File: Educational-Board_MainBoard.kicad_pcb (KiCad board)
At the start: 2 copper layers, 164.5 x 75 mm, 209 parts, among them J201 Screw_Terminal_01x02_P5mm, J202 USB-C_304A-ACP16X, J401 ACC_INT1, J402 BME_SPI, J403 LUX_INT, J501 RGB_OUT, J601 PWR_IN1, J602 PWR_IN2, J603 PWR_IN3, J604 PWR_IN4, J605 MCP_INT, J606 5V, J607 GND, J608 3V3, J609 EX_PA, J610 EX_PB, J611 PWR_OUT1, J612 PWR_OUT3, J613 PWR_OUT2, J614 PWR_OUT4, Q501 AO3400A, Q601 IRLML9301TRPBF, Q602 IRLML9301TRPBF, Q603 IRLML9301TRPBF, Q604 IRLML9301TRPBF, SW301 RESET, SW501 BUTTON1, SW502 BUTTON2, SW503 BUTTON3, SW504 BUTTON4, SW505 BUTTON5, U201 TPS5430DDA, U202 NUCLEO64-H503RB, U401 LSM6DS3, U402 BME280, U403 OPT4001, U404 INA2180A2, U406 YK16S-L7.2-B10Ka(32-8)-G-A29, U501 74LVC1G34, U502 SSD1315 OLED 0.98", U601 TLP291-4, U602 TLP291-4, U603 MCP23017_SS

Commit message: Continued the routing
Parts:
- removed the H102 at (236.0, 53.5)
- removed the H103 at (236.0, 121.5)
- removed kibuzzard-69F9CDB6: G***, kibuzzard-69F9CDB6
- added kibuzzard-69FB5140: G***, kibuzzard-69FB5140, F.Cu at (80.3, 56.6)
- added kibuzzard-69FB71BC: G***, kibuzzard-69FB71BC, F.Cu at (225.5, 58.5)
- added kibuzzard-69FB71E5: G***, kibuzzard-69FB71E5, F.Cu at (225.5, 61.2)
- moved R509 72.9 mm to (194.8, 71.5), turned to -90 degrees
- moved C504 71.2 mm to (197.6, 71.5), turned to 90 degrees
- moved R507 64.3 mm to (197.6, 75.1), turned to 90 degrees
- moved R510 56.3 mm to (223.6, 80.7), turned to 0 degrees
- moved C505 56.3 mm to (223.6, 77.7)
- moved R508 55.2 mm to (223.6, 79.2), turned to 0 degrees
- moved R501 40.2 mm to (203.1, 113.1), turned to 180 degrees
- moved R503 39.4 mm to (199.7, 115.8), turned to 0 degrees
- moved R504 37.0 mm to (188.6, 103.5), turned to 0 degrees
- moved C502 36.8 mm to (192.0, 100.8)
- moved R502 36.8 mm to (188.6, 100.8)
- moved C501 36.3 mm to (199.7, 113.1), turned to 180 degrees
- moved SW501 30.0 mm to (207.0, 105.5)
- moved SW503 30.0 mm to (207.0, 75.5)
- moved H102 20.0 mm to (226.5, 53.5)
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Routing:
- net /MCU/BTN_4: track 0.00 -> 194.1 mm, vias 0 -> 2
- net +3V3: track 302.7 -> 410.3 mm, vias 9 -> 6
- net Net-(C506-Pad1): track 3.25 -> 89.0 mm, vias 0 -> 4
- net /MCU/BTN_3: track 0.06 -> 48.1 mm, vias 0 -> 1
- net /UI/BUZZER: track 25.7 -> 63.5 mm
- net /MCU/BTN_1: track 65.0 -> 92.9 mm
- net Net-(C501-Pad1): track 0.00 -> 15.5 mm
- net /MCU/BTN_2: track 0.00 -> 12.6 mm, vias 0 -> 1
- net /MCU/I2C_SCL: track 156.8 -> 166.1 mm, vias 2 -> 4
- net Net-(C502-Pad1): track 0.00 -> 7.48 mm
- net /MCU/I2C_SDA: track 164.4 -> 171.8 mm, vias 4 -> 6
- net Net-(C505-Pad1): track 0.00 -> 5.69 mm
- net Net-(C504-Pad1): track 0.00 -> 5.32 mm
- net /MCU/JOYSTICK_X: track 35.9 -> 40.8 mm
- net /MCU/JOYSTICK_Y: track 21.7 -> 25.5 mm
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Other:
- board size 164.5 x 75 mm -> 155 x 75 mm
- board text added: "C202>5"
- board text added: "C206>8"
- board text added: "R613>16"
- board text removed: "C202-5"
- board text removed: "C206-8"

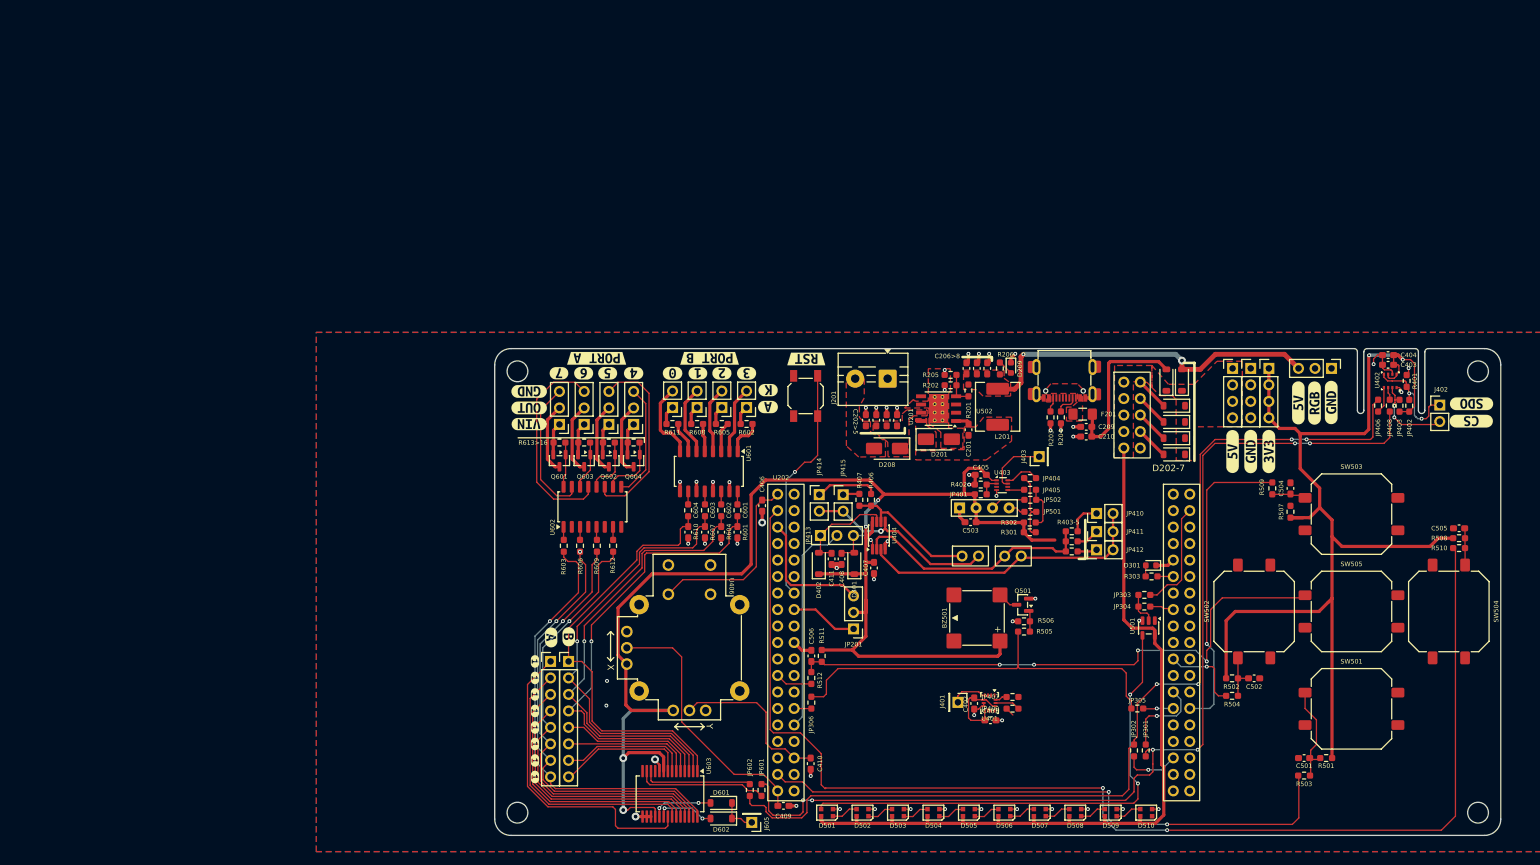
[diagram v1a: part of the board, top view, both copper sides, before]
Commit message: Finished the routing: TODO fixing IMU
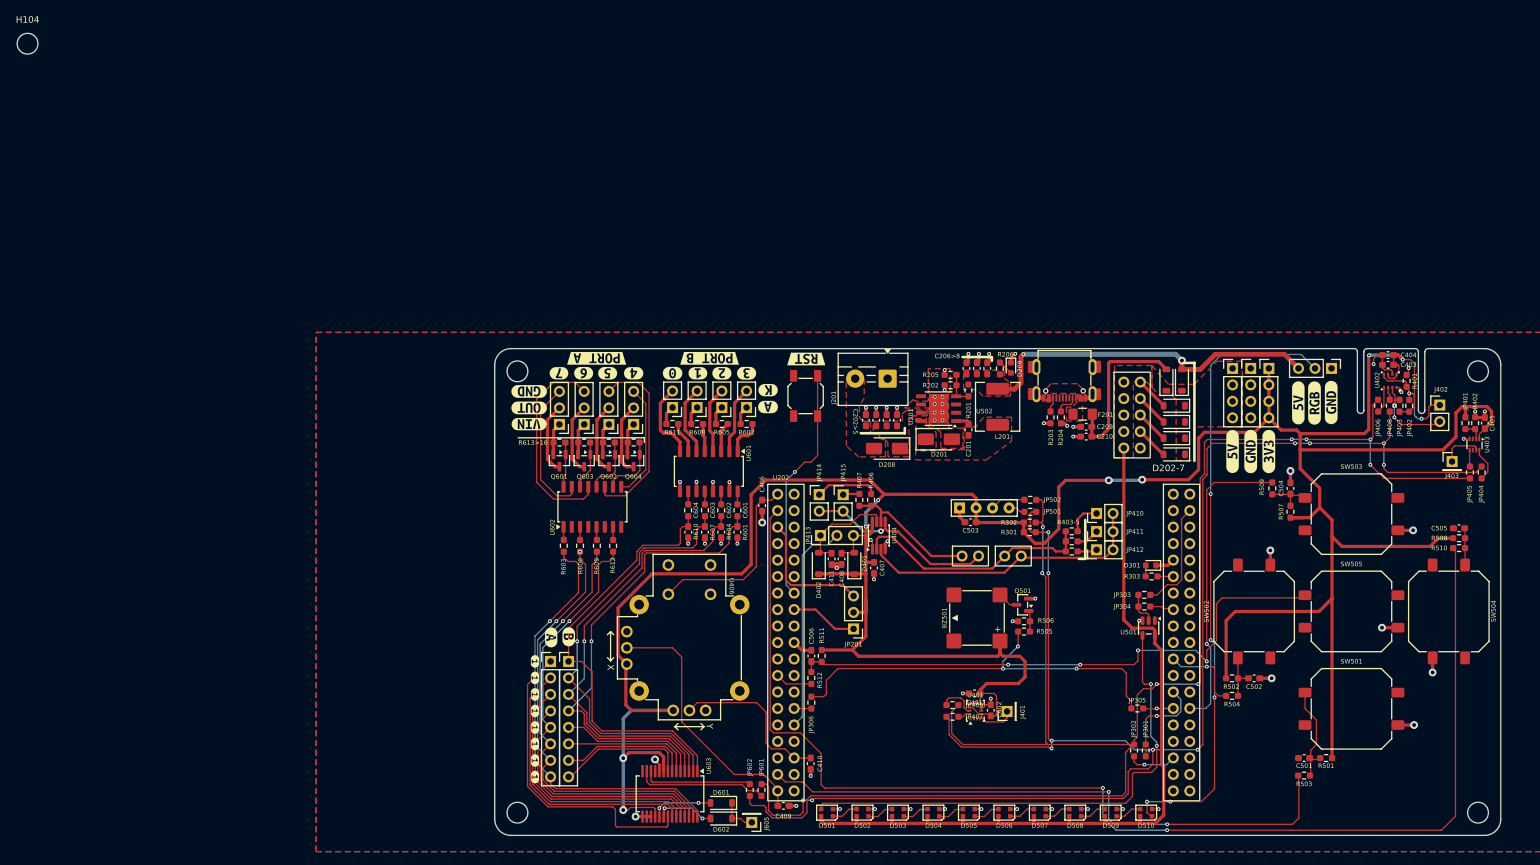
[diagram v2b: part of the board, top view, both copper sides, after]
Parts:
- removed kibuzzard-69FB71BC: G***, kibuzzard-69FB71BC
- removed kibuzzard-69FB71E5: G***, kibuzzard-69FB71E5
- added H104: MountingHole, MountingHole:MountingHole_3.2mm_M3_ISO14580, F.Cu at (3.02, 3.02)
- moved C405 78.1 mm to (227.6, 61.5), turned to 90 degrees
- moved R402 76.8 mm to (226.1, 61.5), turned to 90 degrees
- moved JP401 75.5 mm to (224.6, 61.5), turned to 90 degrees
- moved U403 73.0 mm to (226.0, 64.8), turned to -90 degrees
- moved JP404 69.6 mm to (227.1, 69.1), turned to 90 degrees
- moved JP405 67.8 mm to (225.3, 69.1), turned to -90 degrees
- moved J403 63.6 mm to (222.5, 67.4), turned to 0 degrees
- moved JP407 9.74 mm to (145.5, 106.7), turned to 0 degrees
- moved JP409 9.26 mm to (145.5, 104.9), turned to 0 degrees
- moved J401 7.71 mm to (153.9, 105.9), turned to 90 degrees
- moved C401 4.82 mm to (148.9, 103.1), turned to 180 degrees
- moved C402 2.76 mm to (151.4, 105.7), turned to 90 degrees
- moved U401 2.50 mm to (149.1, 105.8), turned to 90 degrees
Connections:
- U202 pad 18: +5V -> unconnected-(U202A-+5V-Pad18)
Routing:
- net /UI/RGB_OUT: track 0.00 -> 97.0 mm, vias 0 -> 5
- net +3V3: track 410.3 -> 505.4 mm, vias 6 -> 8
- net /MCU/I2C_SCL: track 166.1 -> 253.3 mm, vias 4 -> 8
- net /MCU/I2C_SDA: track 171.8 -> 257.3 mm, vias 6 -> 12
- net GND: track 81.6 -> 97.0 mm, vias 53 -> 58
- net Net-(J403-Pin_1): track 9.49 -> 6.41 mm
- net /UI/RGB_DIN: track 76.3 -> 78.6 mm
- net Net-(JP409-A): track 3.89 -> 5.84 mm
- net Net-(C504-Pad1): track 5.32 -> 7.14 mm
- net /MCU/I2C1_SCL: track 8.65 -> 7.49 mm
- net /MCU/BTN_3: track 48.1 -> 47.3 mm
- net /UI/BUZZER: track 63.5 -> 64.3 mm, vias 0 -> 3

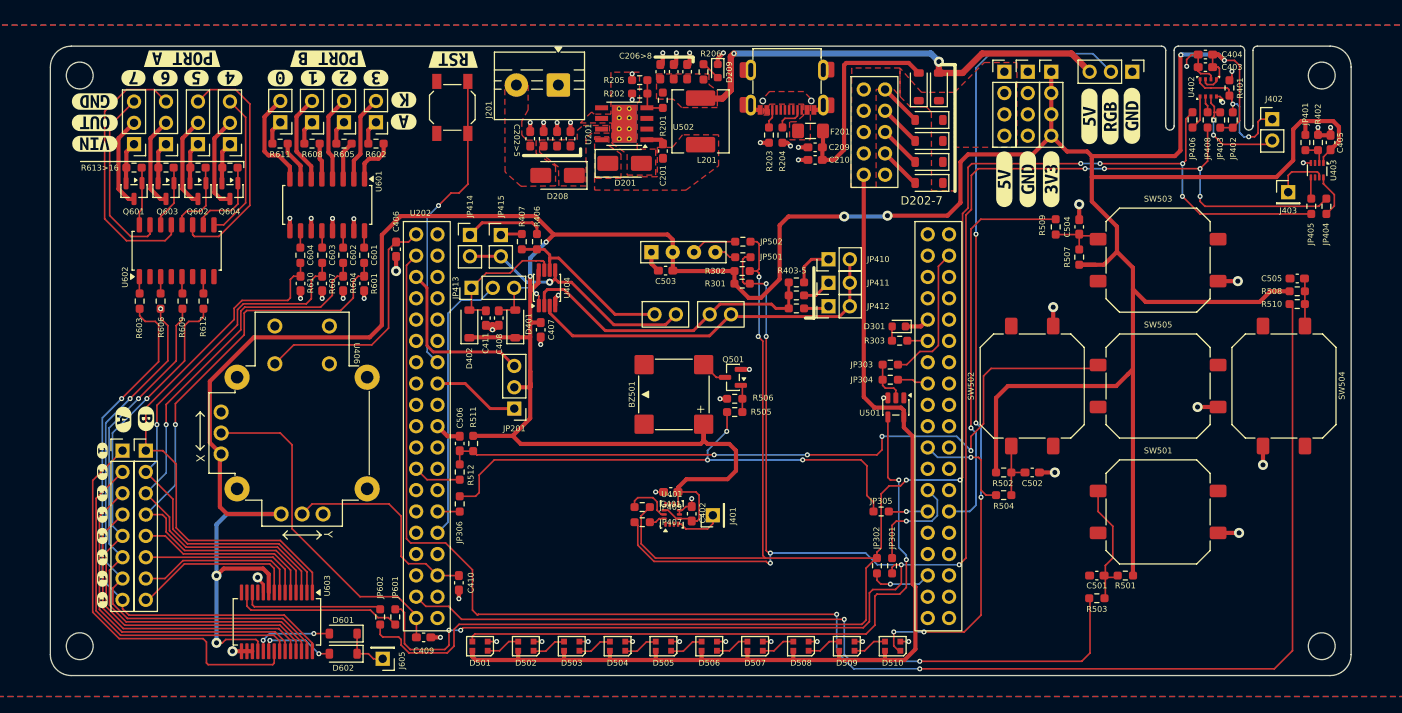
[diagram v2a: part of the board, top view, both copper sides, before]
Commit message: routing and silkscreen logo
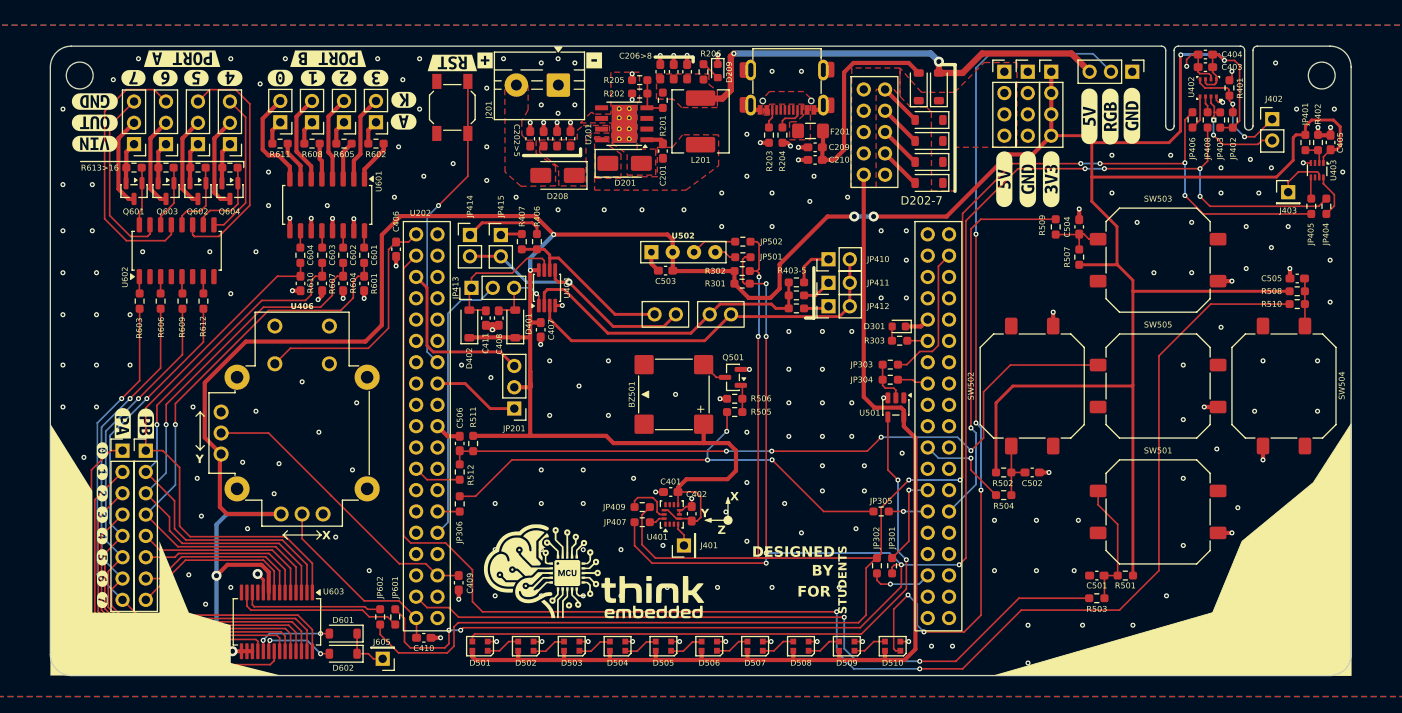
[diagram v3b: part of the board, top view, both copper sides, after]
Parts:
- removed kibuzzard-69F28E96: G***, kibuzzard-69F28E96
- removed kibuzzard-69F28EB1: G***, kibuzzard-69F28EB1
- removed kibuzzard-69F29536 (x8): G***, kibuzzard-69F29536
- added G***: LOGO, LOGO, F.Cu at (140.2, 112.2)
- added G***: LOGO, LOGO, B.Cu at (215.0, 84.1)
- added kibuzzard-69FCC61F: G***, kibuzzard-69FCC61F, F.Cu at (126.8, 51.7)
- added kibuzzard-69FCC630: G***, kibuzzard-69FCC630, F.Cu at (139.8, 51.7)
- added kibuzzard-69FCE761: G***, kibuzzard-69FCE761, F.Cu at (81.2, 98.2)
- added kibuzzard-69FCE768: G***, kibuzzard-69FCE768, F.Cu at (81.2, 100.7)
- added kibuzzard-69FCE76D: G***, kibuzzard-69FCE76D, F.Cu at (81.2, 103.3)
- added kibuzzard-69FCE770: G***, kibuzzard-69FCE770, F.Cu at (81.2, 105.8)
- added kibuzzard-69FCE773: G***, kibuzzard-69FCE773, F.Cu at (81.2, 108.4)
- added kibuzzard-69FCE777: G***, kibuzzard-69FCE777, F.Cu at (81.2, 110.9)
- added kibuzzard-69FCE77B: G***, kibuzzard-69FCE77B, F.Cu at (81.2, 113.5)
- added kibuzzard-69FCE77E: G***, kibuzzard-69FCE77E, F.Cu at (81.2, 116.0)
- added kibuzzard-69FCE792: G***, kibuzzard-69FCE792, F.Cu at (86.4, 95.0)
- added kibuzzard-69FCE79E: G***, kibuzzard-69FCE79E, F.Cu at (83.6, 94.9)
- added kibuzzard-69FCE905: G***, kibuzzard-69FCE905, B.Cu at (208.5, 99.5)
- added kibuzzard-69FCE911: G***, kibuzzard-69FCE911, B.Cu at (206.2, 108.0)
- moved C410 7.77 mm to (119.5, 120.5), turned to 0 degrees
- moved C409 7.73 mm to (123.7, 113.9), turned to -90 degrees
- moved J401 4.98 mm to (150.5, 109.5)
- moved kibuzzard-69F3BF46 0.41 mm to (122.9, 52.0)
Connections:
- C409 pad 1: /MCU/JOYSTICK_X -> /MCU/JOYSTICK_Y
- C410 pad 1: /MCU/JOYSTICK_Y -> /MCU/JOYSTICK_X
- U406 pad 2: /MCU/JOYSTICK_X -> /MCU/JOYSTICK_Y
- U406 pad 5: /MCU/JOYSTICK_Y -> /MCU/JOYSTICK_X
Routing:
- net /MCU/JOYSTICK_X: track 40.8 -> 22.8 mm
- net +3V3: track 505.4 -> 489.4 mm
- net /MCU/BTN_4: track 194.1 -> 184.2 mm
- net /MCU/JOYSTICK_Y: track 25.5 -> 35.4 mm
- net /UI/RGB_OUT: track 97.0 -> 103.9 mm
- net /MCU/I2C_SDA: track 257.3 -> 251.5 mm
- net GND: track 97.0 -> 91.8 mm, vias 58 -> 261
- net /MCU/I2C_SCL: track 253.3 -> 248.8 mm
- net /MCU/BTN_1: track 92.9 -> 88.7 mm
- net /UI/BUZZER: track 64.3 -> 60.3 mm
- net Net-(J401-Pin_1): track 5.63 -> 2.83 mm
- net Net-(C506-Pad1): track 89.0 -> 86.5 mm
- net /UI/RGB_DIN: track 78.6 -> 76.1 mm
- net /POWER_UI/PB3: track 72.0 -> 69.7 mm
- net /MCU/I2C1_SDA: track 13.3 -> 11.2 mm
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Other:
- board text added: "&"
- board text added: "BY"
- board text added: "DESIGNED"
- board text added: "Designed by:"
- board text added: "FOR"
- board text added: "STUDENTS"
- board text added: "X"
- board text added: "Y"
- board text added: "Z"

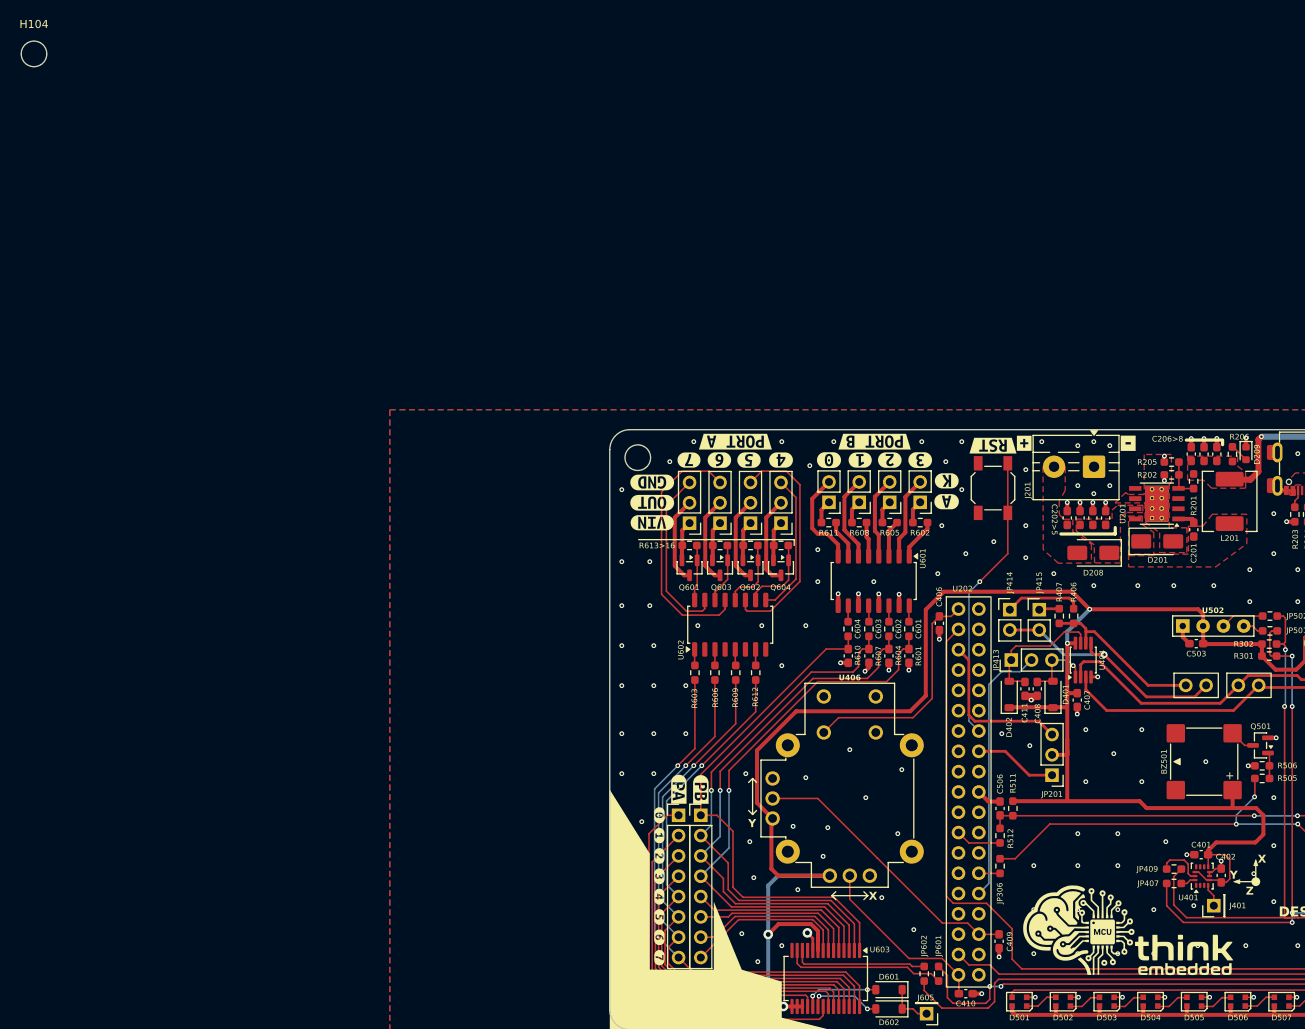
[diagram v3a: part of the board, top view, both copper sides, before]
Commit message: Added pullup to the joystick, Fixes #16
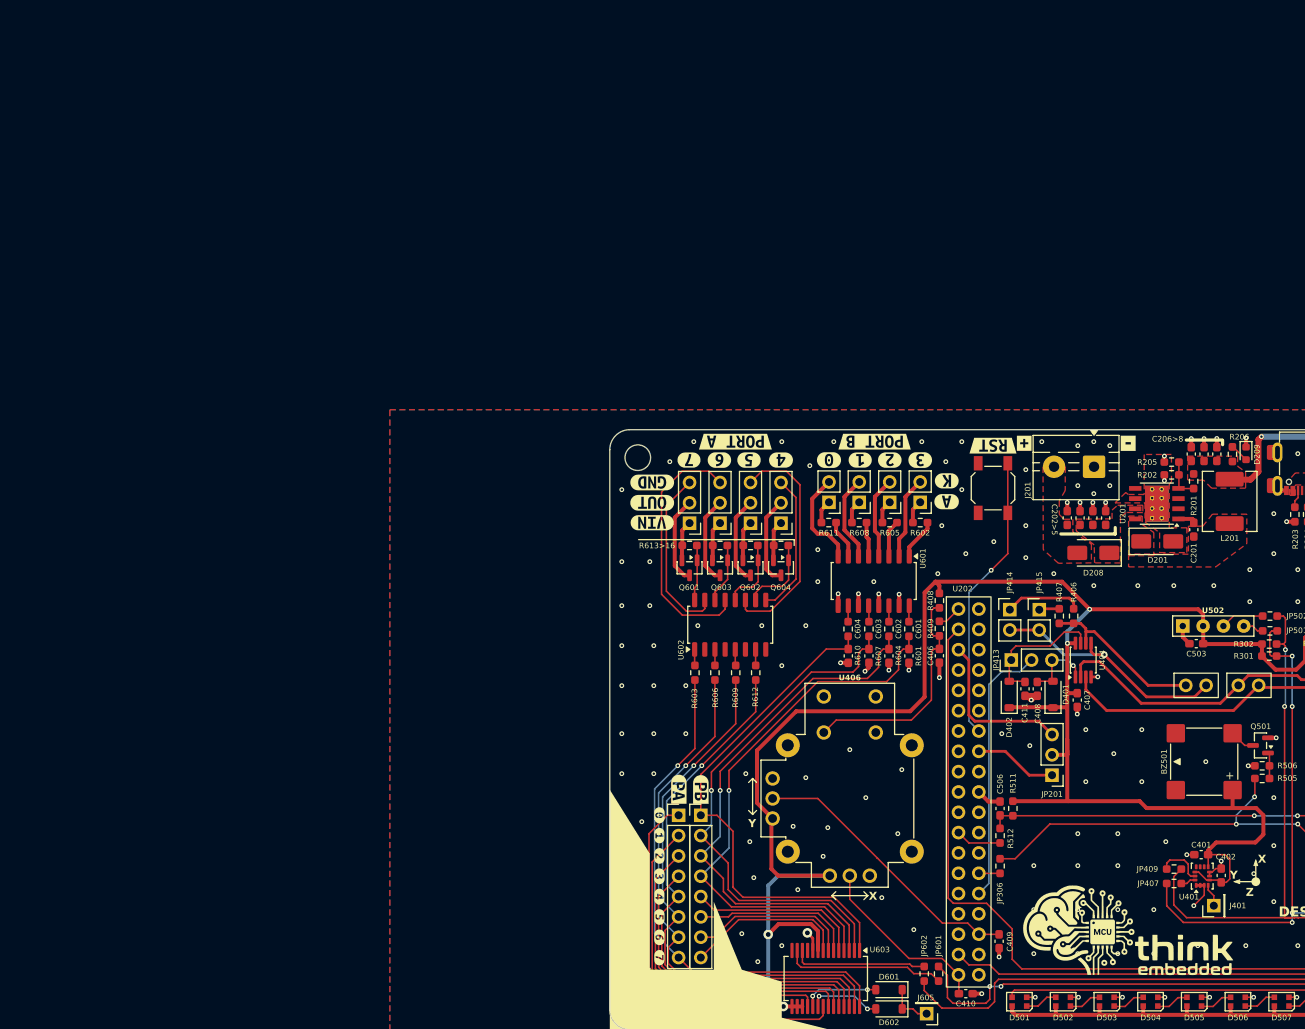
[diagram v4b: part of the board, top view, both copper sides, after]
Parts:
- removed the H104 at (78.5, 121.5)
- removed kibuzzard-69FCE905: G***, kibuzzard-69FCE905
- added R408: 5K1, Resistor_SMD:R_0603_1608Metric_Pad0.98x0.95mm_HandSolder, F.Cu at (116.2, 71.4)
- added R409: 10K, Resistor_SMD:R_0603_1608Metric_Pad0.98x0.95mm_HandSolder, F.Cu at (116.2, 74.9)
- added kibuzzard-69FDFC10: G***, kibuzzard-69FDFC10, B.Cu at (206.8, 99.4)
- moved H104 140.5 mm to (78.5, 121.5)
- moved C406 4.06 mm to (116.2, 78.3)
- moved kibuzzard-69FCE911 0.61 mm to (206.8, 108.2)
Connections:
- C406 pad 1: /MCU/JOYSTICK_BTN -> Net-(C406-Pad1)
- U406 pad 8: /MCU/JOYSTICK_BTN -> Net-(C406-Pad1)
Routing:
- net Net-(C406-Pad1): track 0.00 -> 29.1 mm
- net /MCU/JOYSTICK_BTN: track 28.7 -> 3.41 mm
- net GND: track 91.8 -> 96.6 mm
- net +3V3: track 489.4 -> 493.4 mm
